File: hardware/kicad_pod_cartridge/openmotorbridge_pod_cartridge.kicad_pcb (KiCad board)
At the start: 2 copper layers, 35 x 25 mm, 11 parts, among them J1 POD_BASE_SOCKET_6P, J2 JST_SH_6P_AXIAL, U1 DS2401

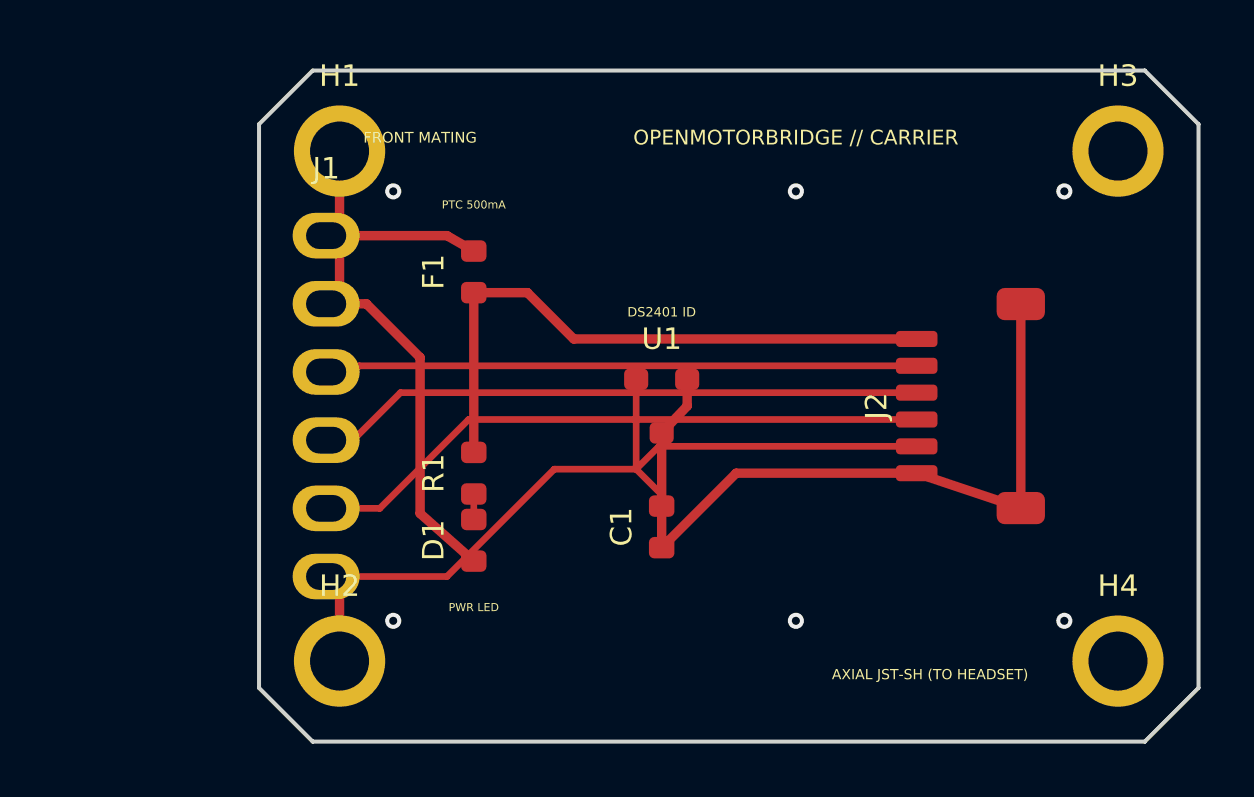
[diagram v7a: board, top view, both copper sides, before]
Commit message: feat(hardware): finalize clean re-routing of pod cartridge adapter PCB without dangling GND vias
- Re-routed openmotorbridge_pod_cartridge.kicad_pcb with 100% connectivity and 0 unrouted nets.
- Removed redundant/dangling ground vias and orphan stubs.
- Verified KiCad DRC: 0 unconnected items and 0 electrical violations.
- Re-rendered 3D top/bottom PCB images.
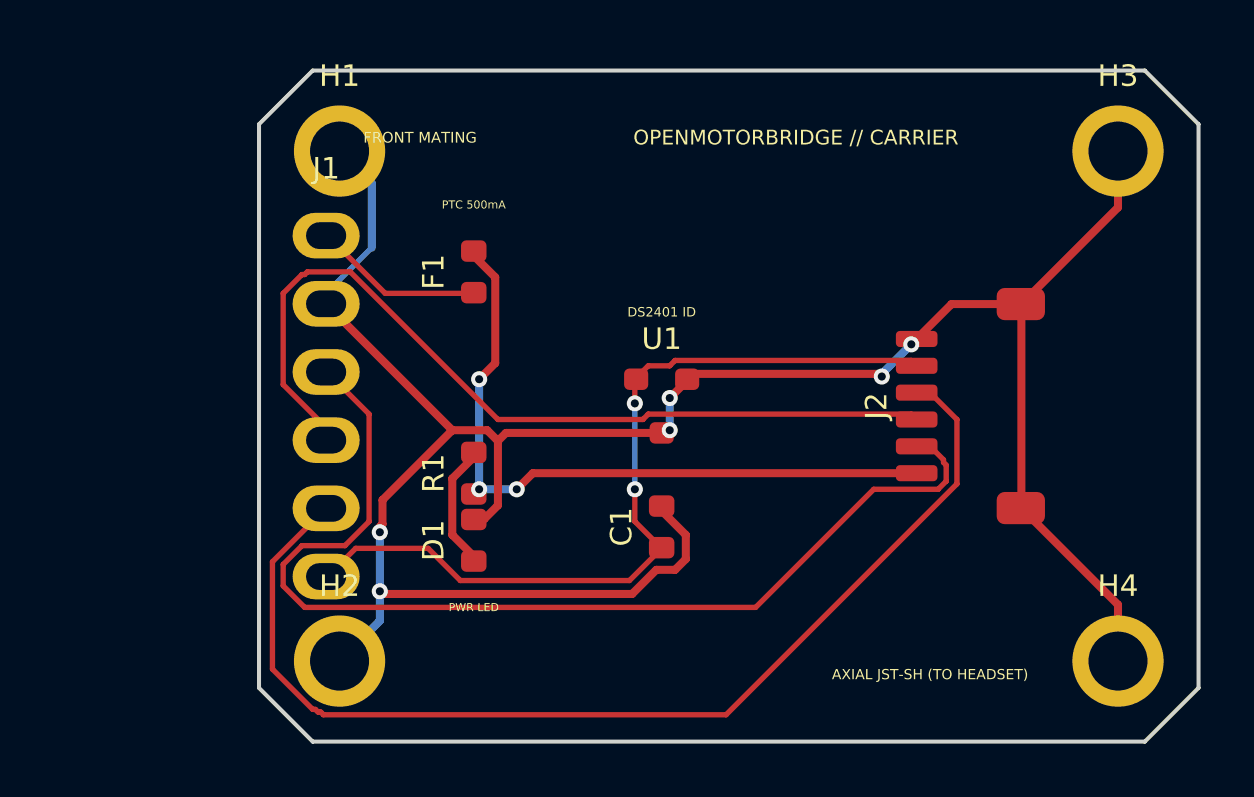
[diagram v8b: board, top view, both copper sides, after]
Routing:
- net GND: track 51.1 -> 87.5 mm
- net POD_NF_P: track 22.1 -> 40.0 mm
- net POD_OPTO_KEY: track 23.4 -> 40.9 mm
- net POD_NF_N: track 22.7 -> 32.0 mm
- net NET_LED_R: track 0.95 -> 4.81 mm
- net VCC_5V_PROT: track 23.2 -> 26.4 mm, vias 0 -> 3
- net POD_1WIRE_ID: track 29.1 -> 31.6 mm, vias 0 -> 2
- net POD_VCC: track 5.65 -> 6.44 mm
